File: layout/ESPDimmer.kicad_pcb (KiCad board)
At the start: 2 copper layers, 36 x 31 mm, 11 parts, among them P1 CONN_01X03, P2 Serial, P3 LED, P4 ProgMod, P5 DS18B20, Q1 Q_NMOS_GDS, U1 LD1117S33CTR, U2 ESP-12E

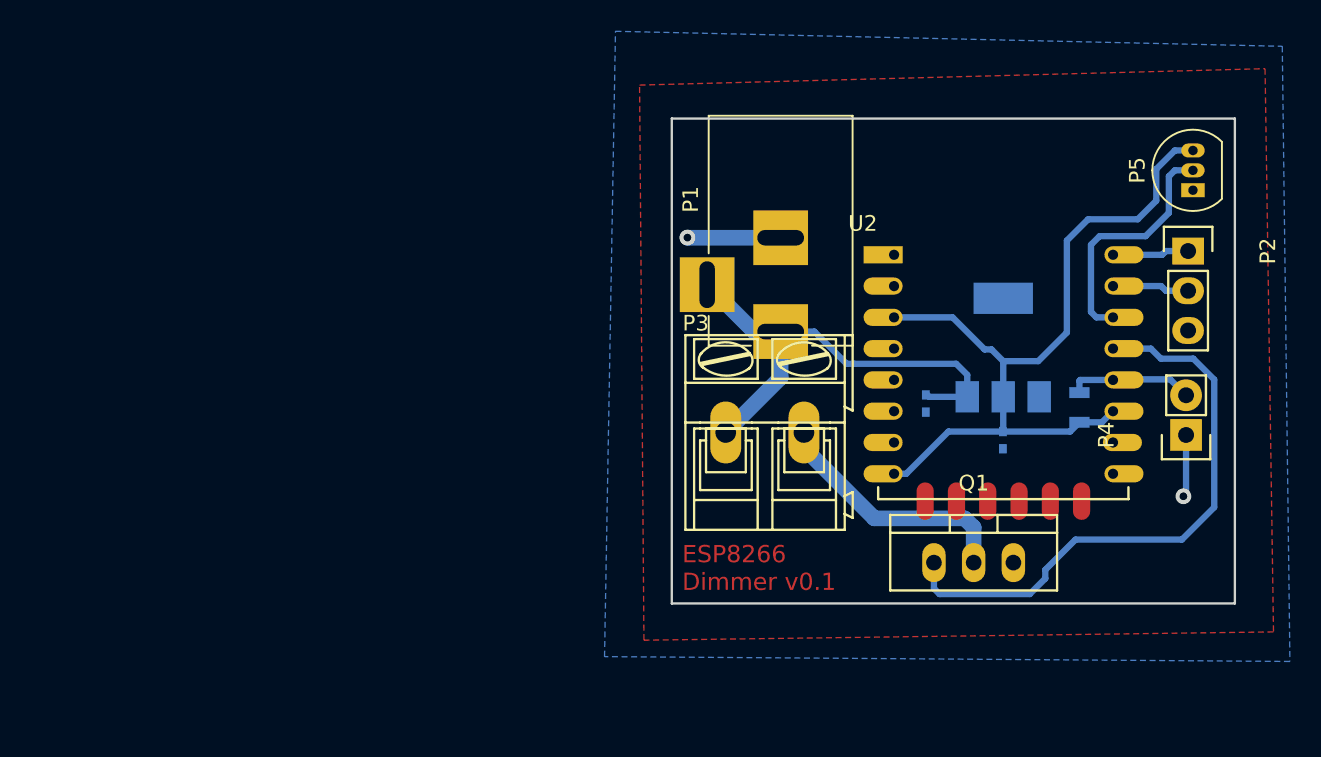
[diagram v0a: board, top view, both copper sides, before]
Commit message: Updated part names and corrected the power supply traces that were shorted!
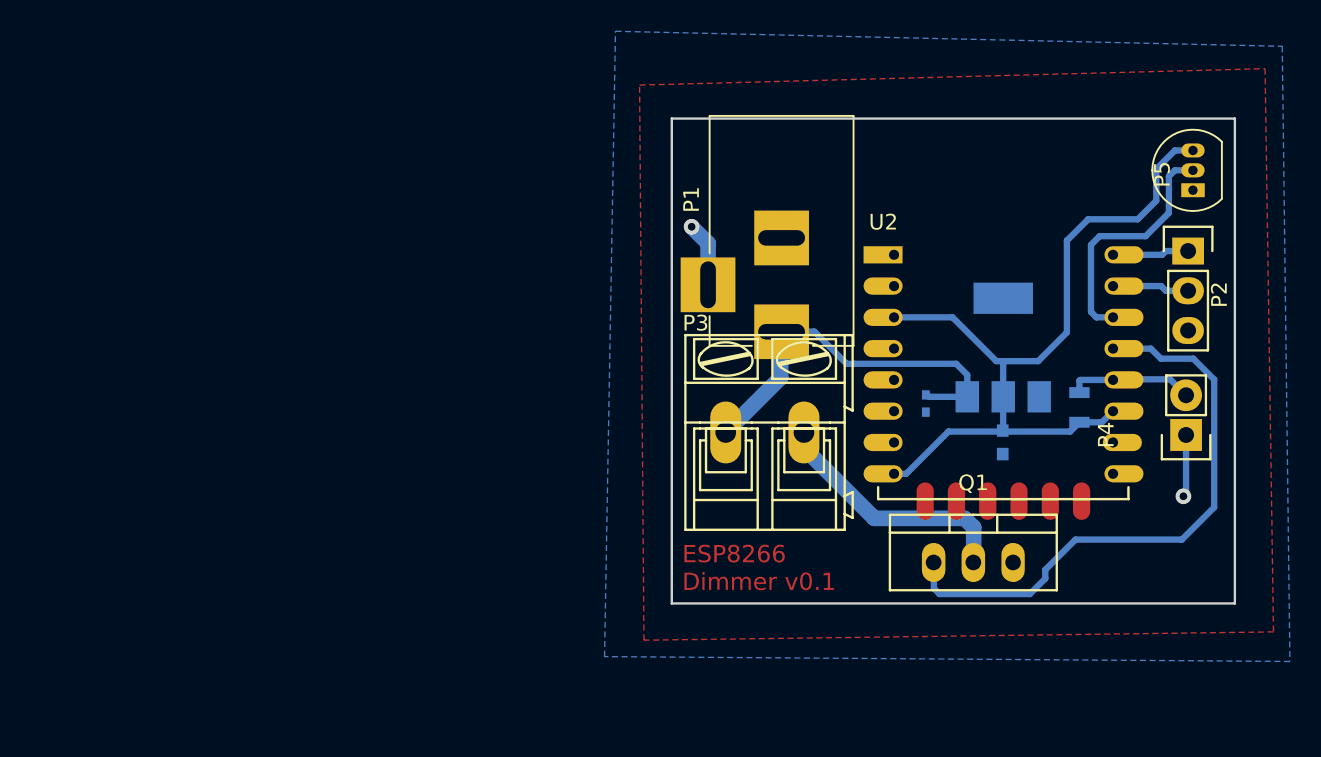
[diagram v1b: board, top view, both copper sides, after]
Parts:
- C2: footprint Capacitors_SMD:C_0402 -> Capacitors_SMD:C_0603
- Q1: value Q_NMOS_GDS -> IRLB8721
- U1: value LD1117S33CTR -> TLV1117-33
- moved C2 0.14 mm to (179.2, 95.7)
- moved P1 0.06 mm to (165.0, 88.6)
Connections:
- P1 pad 3: VCC -> GND
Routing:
- net VCC: track 31.0 -> 25.1 mm
- net GND: track 9.95 -> 8.14 mm

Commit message: Added some vias for better grounding
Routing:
- net GND: track 8.14 -> 26.7 mm, vias 2 -> 5
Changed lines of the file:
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@@
-(kicad_pcb (version 4) (host pcbnew 4.0.4-stable)
+(kicad_pcb (version 4) (host pcbnew "(2016-05-05 BZR 6775)-product")
   (general
     (links 26)
-    (no_connects 4)
+    (no_connects 0)
     (area 153.7 69.42 197.520001 109.710001)
     (thickness 1.6)
     (drawings 5)
-    (tracks 78)
+    (tracks 89)
     (zones 0)
     (modules 11)
@@
   )
   (setup
-    (last_trace_width 1)
+    (last_trace_width 0.25)
     (user_trace_width 0.405)
     (user_trace_width 1)
@@
       (hpglpenspeed 20)
       (hpglpendiameter 15)
-      (hpglpenoverlay 2)
       (psnegative false)
       (psa4output false)
@@
     (descr "DC Barrel Jack")
     (tags "Power Jack")
-    (fp_text reference P1 (at -8.45 5.75 450) (layer F.SilkS)
+    (fp_text reference P1 (at -8.45 5.75 90) (layer F.SilkS)
       (effects (font (size 1 1) (thickness 0.15)))
     )
@@
   (segment (start 164.96 91.56) (end 161.45 95.07) (width 1) (layer B.Cu) (net 1))
   (segment (start 176.89 92.79) (end 174.45 92.79) (width 0.405) (layer B.Cu) (net 1))
+  (segment (start 179.82 103.38) (end 184.08 103.38) (width 0.25) (layer F.Cu) (net 2))
+  (segment (start 184.08 103.38) (end 184.48 103.78) (width 0.25) (layer F.Cu) (net 2))
+  (via (at 184.48 103.78) (size 1) (drill 0.5) (layers F.Cu B.Cu) (net 2))
+  (segment (start 179.39968 101.46) (end 172.72 101.46) (width 0.25) (layer F.Cu) (net 2))
+  (segment (start 172.72 101.46) (end 170.8 103.38) (width 0.25) (layer F.Cu) (net 2))
+  (via (at 170.8 103.38) (size 1) (drill 0.5) (layers F.Cu B.Cu) (net 2))
+  (segment (start 179.82 103.38) (end 179.82 101.88032) (width 0.25) (layer F.Cu) (net 2))
+  (segment (start 179.82 101.88032) (end 179.39968 101.46) (width 0.25) (layer F.Cu) (net 2))
+  (segment (start 191.32 79.58) (end 191.32 79.88) (width 0.25) (layer B.Cu) (net 2))
+  (segment (start 191.32 79.88) (end 192.72 81.28) (width 0.25) (layer B.Cu) (net 2))
+  (via (at 192.72 81.28) (size 1) (drill 0.5) (layers F.Cu B.Cu) (net 2))
   (segment (start 160.32 85.63) (end 160.32 82.97) (width 1) (layer B.Cu) (net 2))
   (segment (start 160.32 82.97) (end 159.27 81.92) (width 1) (layer B.Cu) (net 2))

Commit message: Updated capacitors and other small changes
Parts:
- added C3: 1u, Capacitors_SMD:C_0402, B.Cu at (140.7, 99.7)
- C2: value 10u -> 100n; footprint Capacitors_SMD:C_0603 -> Capacitors_SMD:C_0402
- moved C1 36.9 mm to (137.6, 97.3)
- moved P1 36.9 mm to (128.4, 92.7)
- moved P4 36.9 mm to (154.2, 99.3)
- moved P5 36.9 mm to (154.7, 83.7)
- moved Q1 36.9 mm to (140.6, 107.5)
- moved R1 36.9 mm to (147.4, 97.6)
- moved U1 36.9 mm to (142.5, 93.7)
- moved U2 36.9 mm to (135.6, 87.8)
- moved P3 36.9 mm to (124.8, 99.2)
- moved P2 36.9 mm to (154.4, 87.6)
- moved C2 36.8 mm to (142.5, 99.7)
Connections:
- U2 pad 1: Net-(U2-Pad1) -> (no net)
- U2 pad 17: Net-(U2-Pad17) -> (no net)
- U2 pad 18: Net-(U2-Pad18) -> (no net)
- U2 pad 19: Net-(U2-Pad19) -> (no net)
- U2 pad 2: Net-(U2-Pad2) -> (no net)
- U2 pad 20: Net-(U2-Pad20) -> (no net)
- U2 pad 21: Net-(U2-Pad21) -> (no net)
- U2 pad 22: Net-(U2-Pad22) -> (no net)
- U2 pad 4: Net-(U2-Pad4) -> (no net)
- U2 pad 5: Net-(U2-Pad5) -> (no net)
- U2 pad 6: Net-(U2-Pad6) -> (no net)
- U2 pad 7: Net-(U2-Pad7) -> (no net)
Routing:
- net /-V: track 16.2 -> 19.2 mm
- net +3V3: track 50.6 -> 52.3 mm

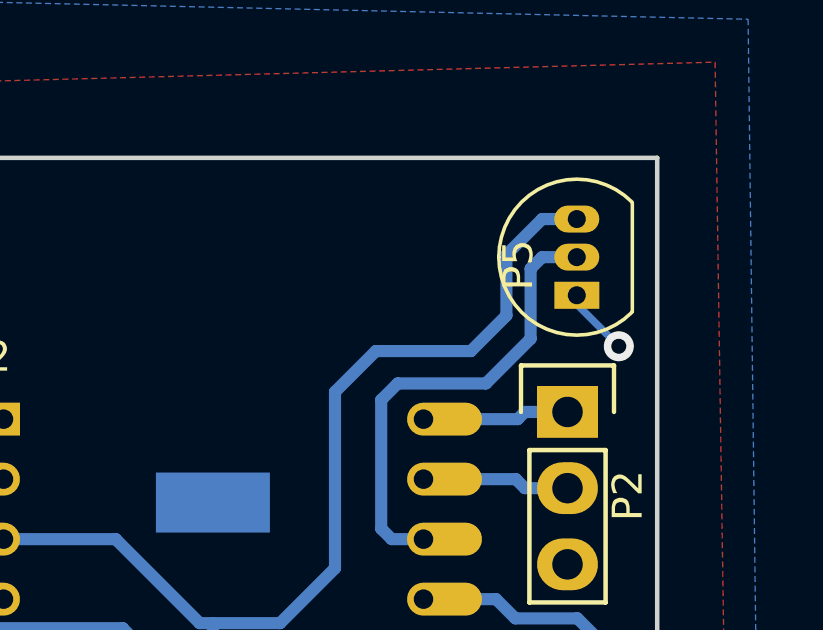
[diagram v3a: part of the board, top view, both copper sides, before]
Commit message: Added pull-up resistor needed for the OneWire communication with the DS18B20 thermometer.
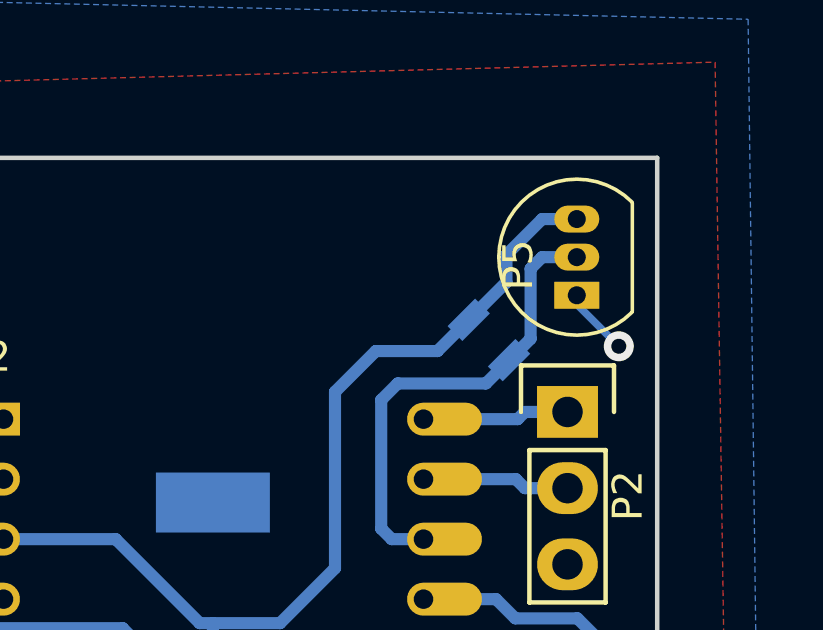
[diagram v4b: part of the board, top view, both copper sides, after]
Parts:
- added R2: 4k7, Resistors_SMD:R_0805, B.Cu at (151.7, 85.2)
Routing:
- net +3V3: track 52.3 -> 51.7 mm
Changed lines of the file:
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@@
 (kicad_pcb (version 4) (host pcbnew "(2016-05-05 BZR 6775)-product")
   (general
-    (links 28)
-    (no_connects 0)
-    (area 153.7 69.42 197.520001 109.710001)
+    (links 30)
+    (no_connects 2)
+    (area 121.274999 79.024999 157.425001 110.175001)
     (thickness 1.6)
     (drawings 5)
-    (tracks 91)
+    (tracks 92)
     (zones 0)
-    (modules 12)
+    (modules 13)
     (nets 10)
   )
@@
   )
   (setup
-    (last_trace_width 0.25)
+    (last_trace_width 0.405)
     (user_trace_width 0.405)
     (user_trace_width 1)
@@
     (descr "DC Barrel Jack")
     (tags "Power Jack")
-    (fp_text reference P1 (at -8.45 5.75 450) (layer F.SilkS)
+    (fp_text reference P1 (at -8.45 5.75 90) (layer F.SilkS)
       (effects (font (size 1 1) (thickness 0.15)))
     )
@@
       (net 2 GND))
     (model Capacitors_SMD.3dshapes/C_0402.wrl
+      (at (xyz 0 0 0))
+      (scale (xyz 1 1 1))
+      (rotate (xyz 0 0 0))
+    )
+  )
+  (module Resistors_SMD:R_0805 (layer B.Cu)
+    (at 151.74 85.17 135)
+    (descr "Resistor SMD 0805, reflow soldering, Vishay (see dcrcw.pdf)")
+    (tags "resistor 0805")
+    (attr smd)
+    (fp_text reference R2 (at 0 2.1 135) (layer B.SilkS)
+      (effects (font (size 1 1) (thickness 0.15)) (justify mirror))
+    )
+    (fp_text value 4k7 (at 0 -2.1 135) (layer B.Fab)
+      (effects (font (size 1 1) (thickness 0.15)) (justify mirror))
+    )
+    (fp_line (start -1 -0.625) (end -1 0.625) (layer B.Fab) (width 0.1))
+    (fp_line (start 1 -0.625) (end -1 -0.625) (layer B.Fab) (width 0.1))
+    (fp_line (start 1 0.625) (end 1 -0.625) (layer B.Fab) (width 0.1))
+    (fp_line (start -1 0.625) (end 1 0.625) (layer B.Fab) (width 0.1))
+    (fp_line (start -1.6 1) (end 1.6 1) (layer B.CrtYd) (width 0.05))
+    (fp_line (start -1.6 -1) (end 1.6 -1) (layer B.CrtYd) (width 0.05))
+    (fp_line (start -1.6 1) (end -1.6 -1) (layer B.CrtYd) (width 0.05))
+    (fp_line (start 1.6 1) (end 1.6 -1) (layer B.CrtYd) (width 0.05))
+    (fp_line (start 0.6 -0.875) (end -0.6 -0.875) (layer B.SilkS) (width 0.15))
+    (fp_line (start -0.6 0.875) (end 0.6 0.875) (layer B.SilkS) (width 0.15))
+    (pad 1 smd rect (at -0.95 0 135) (size 0.7 1.3) (layers B.Cu B.Paste B.Mask)
+      (net 9 "Net-(P5-Pad2)"))
+    (pad 2 smd rect (at 0.95 0 135) (size 0.7 1.3) (layers B.Cu B.Paste B.Mask)
+      (net 3 +3V3))
+    (model Resistors_SMD.3dshapes/R_0805.wrl
       (at (xyz 0 0 0))
       (scale (xyz 1 1 1))
@@
   (segment (start 154.23 103.08) (end 154.06 103.25) (width 0.405) (layer B.Cu) (net 2))
   (via (at 154.06 103.25) (size 1) (drill 0.5) (layers F.Cu B.Cu) (net 2))
+  (segment (start 147.97 85.54) (end 150.026498 85.54) (width 0.405) (layer B.Cu) (net 3))
+  (segment (start 150.026498 85.54) (end 151.068249 84.498249) (width 0.405) (layer B.Cu) (net 3))
+  (segment (start 152.32443 82.33) (end 152.32443 83.242068) (width 0.405) (layer B.Cu) (net 3))
+  (segment (start 152.32443 83.242068) (end 151.068249 84.498249) (width 0.405) (layer B.Cu) (net 3))
   (segment (start 140.74 99.11) (end 139.04 99.11) (width 0.405) (layer B.Cu) (net 3))
   (segment (start 142.54 94.61) (end 142.1 94.61) (width 0.405) (layer B.Cu) (net 3))
@@
   (segment (start 146.61 86.9) (end 146.61 92.78) (width 0.405) (layer B.Cu) (net 3))
   (segment (start 147.97 85.54) (end 146.61 86.9) (width 0.405) (layer B.Cu) (net 3))
-  (segment (start 151.14 85.54) (end 147.97 85.54) (width 0.405) (layer B.Cu) (net 3))
-  (segment (start 152.32443 84.35557) (end 151.14 85.54) (width 0.405) (layer B.Cu) (net 3))
-  (segment (start 152.32443 82.33) (end 152.32443 84.35557) (width 0.405) (layer B.Cu) (net 3))
   (segment (start 154.67 81.14) (end 153.51443 81.14) (width 0.405) (layer B.Cu) (net 3))
   (segment (start 153.51443 81.14) (end 152.32443 82.33) (width 0.405) (layer B.Cu) (net 3))
